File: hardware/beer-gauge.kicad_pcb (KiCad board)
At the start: 2 copper layers, 45 parts, among them P1 CONN_01X04, P2 CONN_01X04, P3 CONN_01X04, P4 CONN_01X04, P5 USB_OTG, SW1 SW_PUSH, U1 ADS1234IPW, U2 LP38691, U3 MKL02Z32, U4 MK20DX256VLH7, Y1 16 MHz, Y2 32.768 kHz

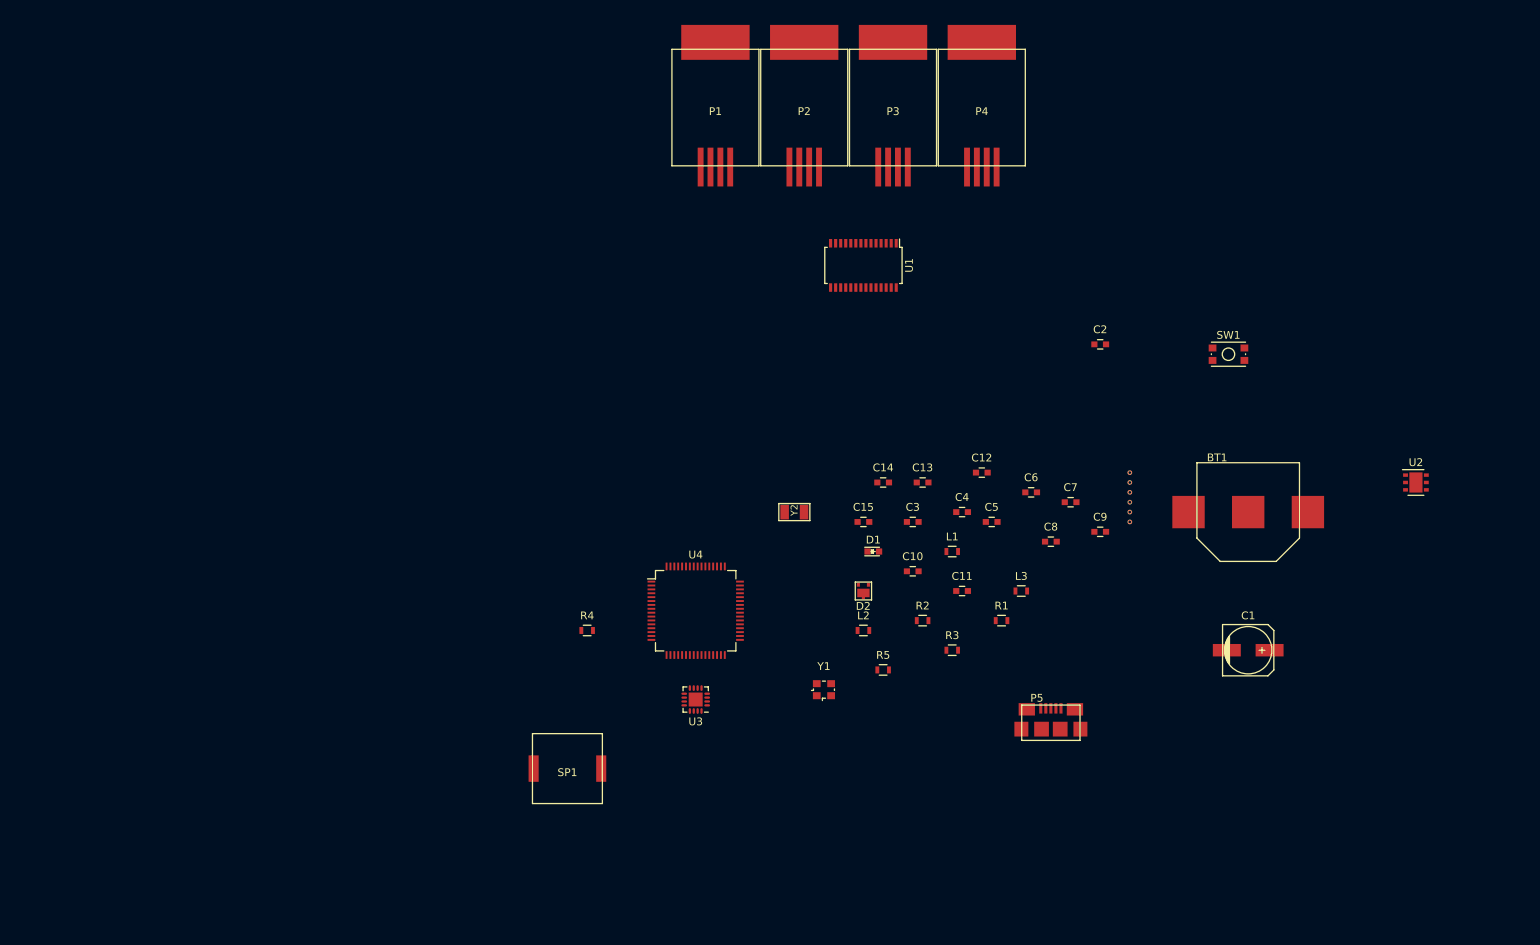
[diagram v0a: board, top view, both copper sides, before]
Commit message: Finished footprints.  Switched to a tantalum cap for the LCD.  Changed piezo resistor value to 470 to reduce part count.
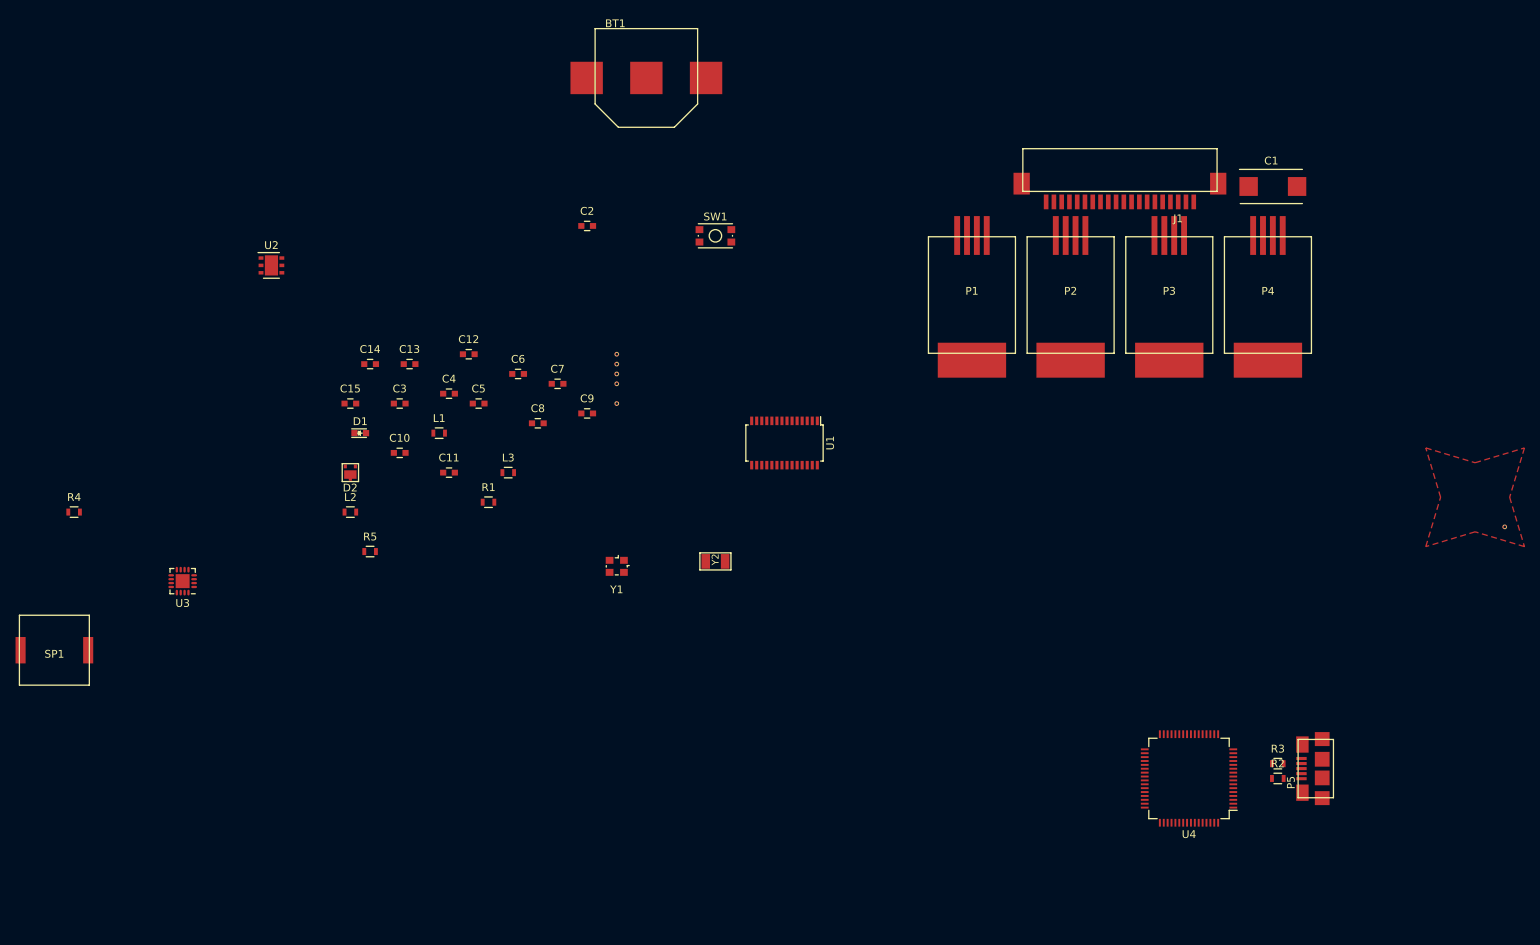
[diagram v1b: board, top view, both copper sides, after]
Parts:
- added J1: OLED_MODULE, footprint:0522712069, F.Cu at (165.1, 57.8)
- C1: footprint Capacitors_SMD:c_elec_6.3x5.8 -> Capacitors_Tantalum_SMD:TantalC_SizeD_EIA-7343_Reflow
- R5: value 1k -> 470
- moved U2 149.9 mm to (55.9, 67.3)
- moved BT1 95.5 mm to (104.1, 43.2)
- moved C10 67.8 mm to (72.4, 91.4)
- moved C11 67.8 mm to (78.7, 94.0)
- moved C14 67.8 mm to (68.6, 80.0)
- moved C15 67.8 mm to (66.0, 85.1)
- moved C2 67.8 mm to (96.5, 62.2)
- moved C3 67.8 mm to (72.4, 85.1)
- moved C4 67.8 mm to (78.7, 83.8)
- moved C5 67.8 mm to (82.5, 85.1)
- moved C7 67.8 mm to (92.7, 82.5)
- moved C8 67.8 mm to (90.2, 87.6)
- moved C9 67.8 mm to (96.5, 86.4)
- moved D2 67.8 mm to (66.0, 94.0)
- moved L2 67.8 mm to (66.0, 99.1)
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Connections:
- U4 pad 37: (no net) -> /Teensy/19/A5
- U4 pad 38: (no net) -> /Teensy/18/A4
- U4 pad 62: (no net) -> /Teensy/20/A6
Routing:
- added copper zone on F.Cu, net /Teensy/17/A3

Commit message: Working on capacitive touch arrow pad layout
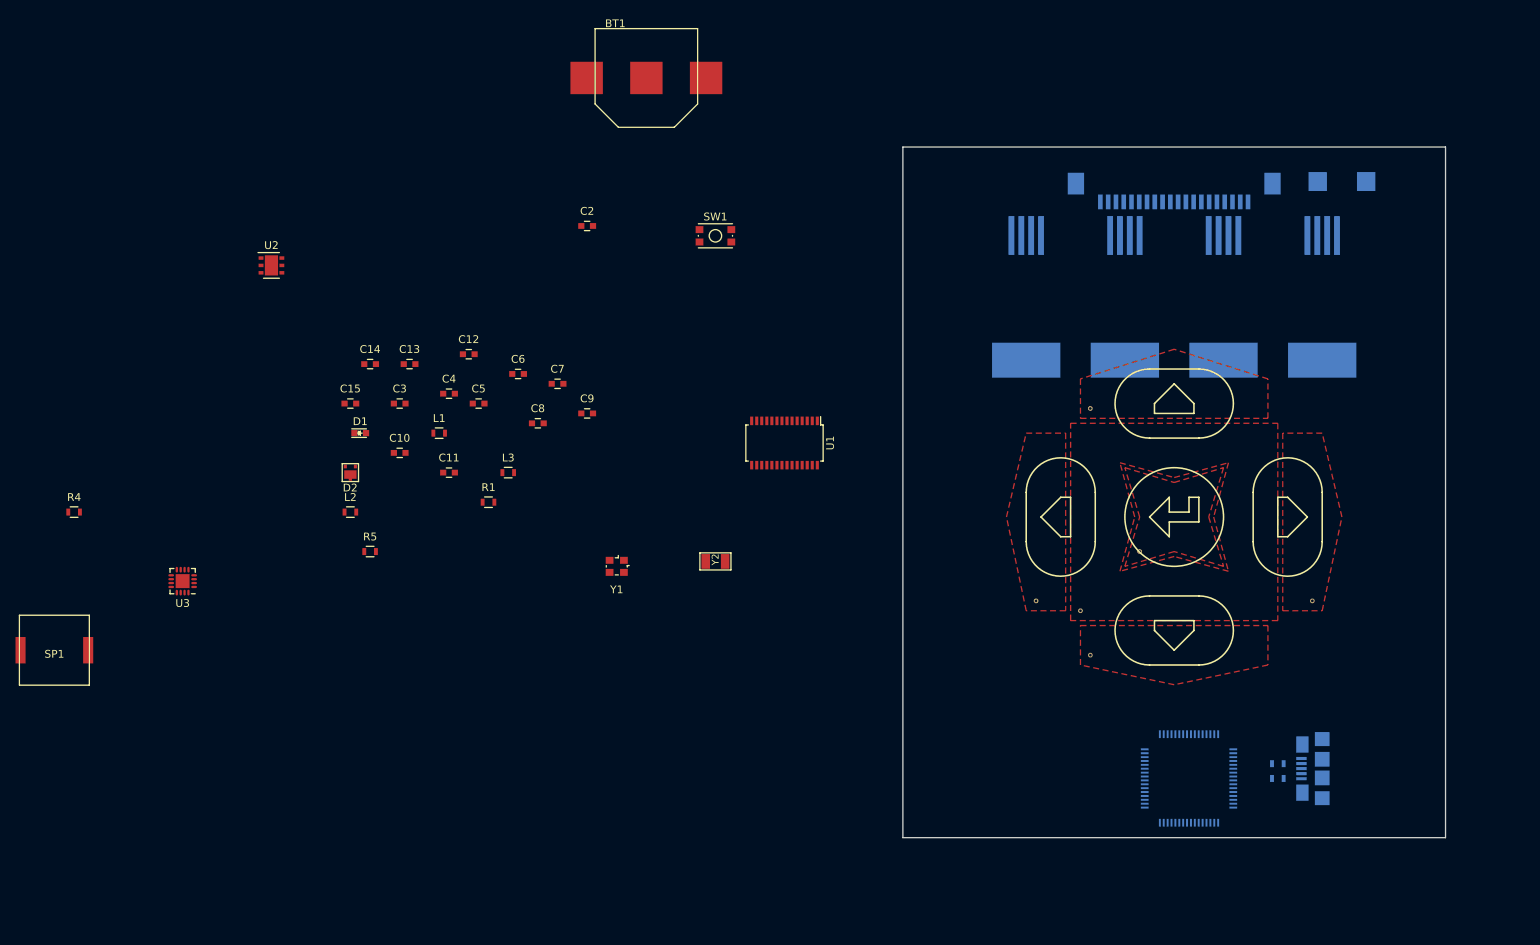
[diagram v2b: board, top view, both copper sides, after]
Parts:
- C1, J1, P1, P2, P3, P4, P5, R2, R3, U4: moved to B.Cu
- moved W4 93.8 mm to (189.9, 110.5)
- moved W2 71.6 mm to (161.3, 117.5)
- moved W6 65.4 mm to (160.0, 111.8)
- moved W3 61.4 mm to (154.3, 110.5)
- moved W1 61.4 mm to (161.3, 85.7)
- moved W5 47.1 mm to (167.6, 104.1)
- moved C1 8.91 mm to (193.7, 56.5)
- moved J1 6.99 mm to (172.1, 57.8), turned to 0 degrees
- moved P2 6.99 mm to (165.7, 71.1), turned to 0 degrees
- moved P3 6.99 mm to (178.4, 71.1), turned to 0 degrees
- moved P1 6.98 mm to (153.0, 71.1), turned to 0 degrees
- moved P4 6.98 mm to (191.1, 71.1), turned to 0 degrees
- turned P5 to 270 degrees
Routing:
- added copper zone on F.Cu, net /Teensy/15/A1
- added copper zone on F.Cu, net /Teensy/16/A2
- added copper zone on F.Cu, net /Teensy/22/A8
- added copper zone on F.Cu, net /Teensy/23/A9
- added copper zone on F.Cu, net /Teensy/25
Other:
- board outline added: 69.8 x 88.9 mm

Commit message: Working on component placement
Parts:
- moved P1 47.0 mm to (200.0, 71.1)
- moved P4 47.0 mm to (144.1, 71.1)
- moved P3 22.9 mm to (155.6, 71.1)
- moved P2 22.9 mm to (188.6, 71.1)
- moved P5 14.0 mm to (205.1, 130.8)
- moved R2 12.8 mm to (198.1, 132.1)
- moved R3 12.8 mm to (198.1, 130.2)
- moved W1 3.86 mm to (161.9, 81.9)
- moved W3 2.69 mm to (152.4, 108.6)
- moved W4 2.69 mm to (191.8, 108.6)
- moved U4 2.29 mm to (172.7, 131.4)
- moved W6 1.27 mm to (160.0, 110.5)
- moved W5 1.27 mm to (167.6, 102.9)
- moved W2 0.90 mm to (161.9, 118.1)
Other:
- net class Default: clearance 0.2 -> 0.1524; trace_width 0.25 -> 0.1524; via_dia 0.6 -> 0.508; via_drill 0.4 -> 0.3302
- rule trace_clearance: 0.2 -> 0.1524
- rule trace_min: 0.2 -> 0.1524
- rule via_min_drill: 0.3 -> 0.3302
- rule via_min_size: 0.4 -> 0.508

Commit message: Working on PCB layout
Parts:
- BT1, C10, C11, C12, C13, C14, C15, C2, C3, C4, C5, C6, C7, C8, C9, D1, D2, L1, L2, L3, R1, R4, R5, SP1, SW1, U1, U2, U3, Y1, Y2: moved to B.Cu
- moved U2 155.7 mm to (201.9, 121.3)
- moved U3 134.2 mm to (176.5, 131.4), turned to 270 degrees
- moved SP1 115.0 mm to (142.9, 119.4), turned to 270 degrees
- moved D2 103.4 mm to (159.4, 138.4), turned to 270 degrees
- moved BT1 101.1 mm to (149.9, 133.3)
- moved SW1 91.8 mm to (169.5, 135.9)
- moved Y2 90.5 mm to (197.5, 137.8), turned to 90 degrees
- moved Y1 84.1 mm to (178.4, 137.2)
- moved U1 79.6 mm to (201.3, 83.8), turned to 0 degrees
- moved C12 78.6 mm to (108.6, 152.4)
- moved C13 76.2 mm to (101.0, 151.1)
- moved C14 76.2 mm to (95.9, 151.1)
- moved C6 73.8 mm to (114.9, 149.9)
- moved R4 72.5 mm to (85.1, 146.7)
- moved C7 71.5 mm to (120.0, 148.6)
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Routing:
- added copper zone on B.Cu, net GND
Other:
- board size 69.8 x 88.9 mm -> 69.8 x 95.2 mm

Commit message: Working on PCB layout
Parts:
- added REF**: MountingHole_3.2mm_M3_Pad, Mounting_Holes:MountingHole_3.2mm_M3_Pad, F.Cu at (202.6, 50.2)
- added REF**: MountingHole_3.2mm_M3_Pad, Mounting_Holes:MountingHole_3.2mm_M3_Pad, F.Cu at (141.6, 50.2)
- added REF**: MountingHole_3.2mm_M3_Pad, Mounting_Holes:MountingHole_3.2mm_M3_Pad, F.Cu at (141.6, 136.5)
- added REF**: MountingHole_3.2mm_M3_Pad, Mounting_Holes:MountingHole_3.2mm_M3_Pad, F.Cu at (202.6, 136.5)
- moved R4 131.9 mm to (203.1, 87.6), turned to 90 degrees
- moved C15 126.9 mm to (203.7, 83.4)
- moved L2 117.1 mm to (203.7, 93.0)
- moved D1 116.7 mm to (205.0, 104.4), turned to 180 degrees
- moved C14 115.0 mm to (186.1, 79.8), turned to 180 degrees
- moved C10 114.7 mm to (203.7, 91.3)
- moved C13 113.0 mm to (199.0, 95.0)
- moved C11 112.8 mm to (203.7, 80.6)
- moved L3 104.0 mm to (203.7, 85.1)
- moved C8 103.7 mm to (204.7, 87.5), turned to 270 degrees
- moved C12 101.8 mm to (190.4, 91.8), turned to 180 degrees
- moved L1 96.8 mm to (200.8, 130.3), turned to 270 degrees
- moved C5 95.8 mm to (201.5, 118.4), turned to 90 degrees
- moved R1 95.4 mm to (202.1, 104.4)
- moved R5 94.2 mm to (179.2, 82.9), turned to 90 degrees
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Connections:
- net Net-(R2-Pad1) renamed /Teensy/USB_D-
- net Net-(R3-Pad1) renamed /Teensy/USB_D+
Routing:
- net +5V: track 0.00 -> 163.3 mm, vias 0 -> 8
- net /Teensy/16/A2: track 0.00 -> 96.0 mm, vias 0 -> 2
- net /Teensy/17/A3: track 0.00 -> 60.4 mm, vias 0 -> 2
- net /Teensy/22/A8: track 0.00 -> 54.5 mm, vias 0 -> 2
- net /Teensy/USB_D-: track 0.00 -> 53.8 mm
- net /Teensy/USB_D+: track 0.00 -> 53.6 mm
- net /Teensy/25: track 0.00 -> 51.1 mm, vias 0 -> 2
- net Net-(P2-Pad2): track 0.00 -> 40.9 mm
- net Net-(P2-Pad3): track 0.00 -> 40.4 mm
- net /Teensy/2: track 0.00 -> 39.5 mm, vias 0 -> 2
- net /Teensy/14/A0: track 0.00 -> 39.4 mm
- net /Teensy/12: track 0.00 -> 34.7 mm
- net /Teensy/23/A9: track 0.00 -> 34.4 mm, vias 0 -> 2
- net /Teensy/15/A1: track 0.00 -> 27.0 mm
- net Net-(P4-Pad3): track 0.00 -> 25.8 mm
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- added copper zone on In1.Cu, net +3V3
- added copper zone on In2.Cu, net GND
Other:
- outline, holes or cut-outs redrawn
- copper layers 2 -> 4
- net class 90Ohm added: clearance 0.127, trace_width 0.2286, via_dia 0.3556, via_drill 0.254
- net class Default: clearance 0.1524 -> 0.127; trace_width 0.1524 -> 0.127; via_dia 0.508 -> 0.3556; via_drill 0.3302 -> 0.254
- net class Power added: clearance 0.2032, trace_width 0.3556, via_dia 0.508, via_drill 0.4064
- rule trace_clearance: 0.1524 -> 0.127
- rule trace_min: 0.1524 -> 0.127
- rule via_min_drill: 0.3302 -> 0.254
- rule via_min_size: 0.508 -> 0.3556

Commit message: Working on PCB layout
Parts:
- moved SW1 1.73 mm to (202.8, 108.8)
- moved D1 1.53 mm to (204.9, 102.9)
- moved C5 1.45 mm to (200.4, 117.5)
- moved C7 1.45 mm to (203.7, 114.6)
- moved U2 1.45 mm to (203.2, 117.2)
- moved R1 1.17 mm to (201.2, 103.6)
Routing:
- net Net-(P1-Pad2): track 0.00 -> 61.8 mm, vias 0 -> 2
- net Net-(P1-Pad3): track 0.00 -> 60.9 mm, vias 0 -> 2
- net /Teensy/20/A6: track 0.00 -> 54.1 mm
- net /Teensy/4: track 0.00 -> 53.6 mm, vias 0 -> 2
- net /Teensy/5: track 0.00 -> 49.8 mm, vias 0 -> 2
- net /Teensy/19/A5: track 0.00 -> 49.0 mm, vias 0 -> 4
- net /Teensy/18/A4: track 0.00 -> 48.5 mm, vias 0 -> 4
- net GND: track 14.6 -> 62.4 mm, vias 13 -> 40
- net /Teensy/3: track 0.00 -> 46.5 mm, vias 0 -> 4
- net /Teensy/0: track 0.00 -> 38.9 mm, vias 0 -> 4
- net /Teensy/1: track 0.00 -> 38.4 mm, vias 0 -> 4
- net Net-(P3-Pad2): track 0.00 -> 33.7 mm, vias 0 -> 2
- net Net-(P3-Pad3): track 0.00 -> 33.3 mm, vias 0 -> 2
- net /Teensy/6: track 0.00 -> 23.2 mm, vias 0 -> 2
- net +3V3: track 16.1 -> 38.9 mm, vias 5 -> 7
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- added copper zone on F.Cu, net GND
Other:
- net class Power removed

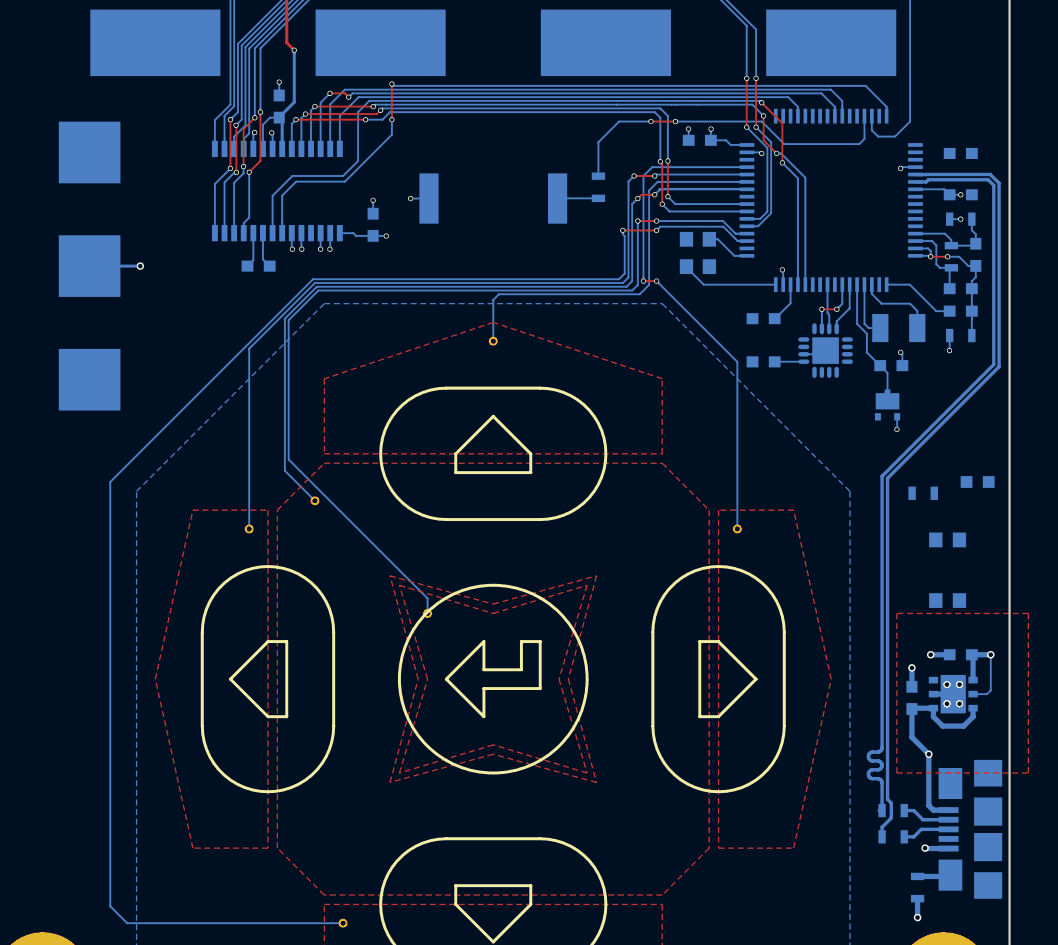
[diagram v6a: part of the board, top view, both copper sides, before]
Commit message: Finished routing traces
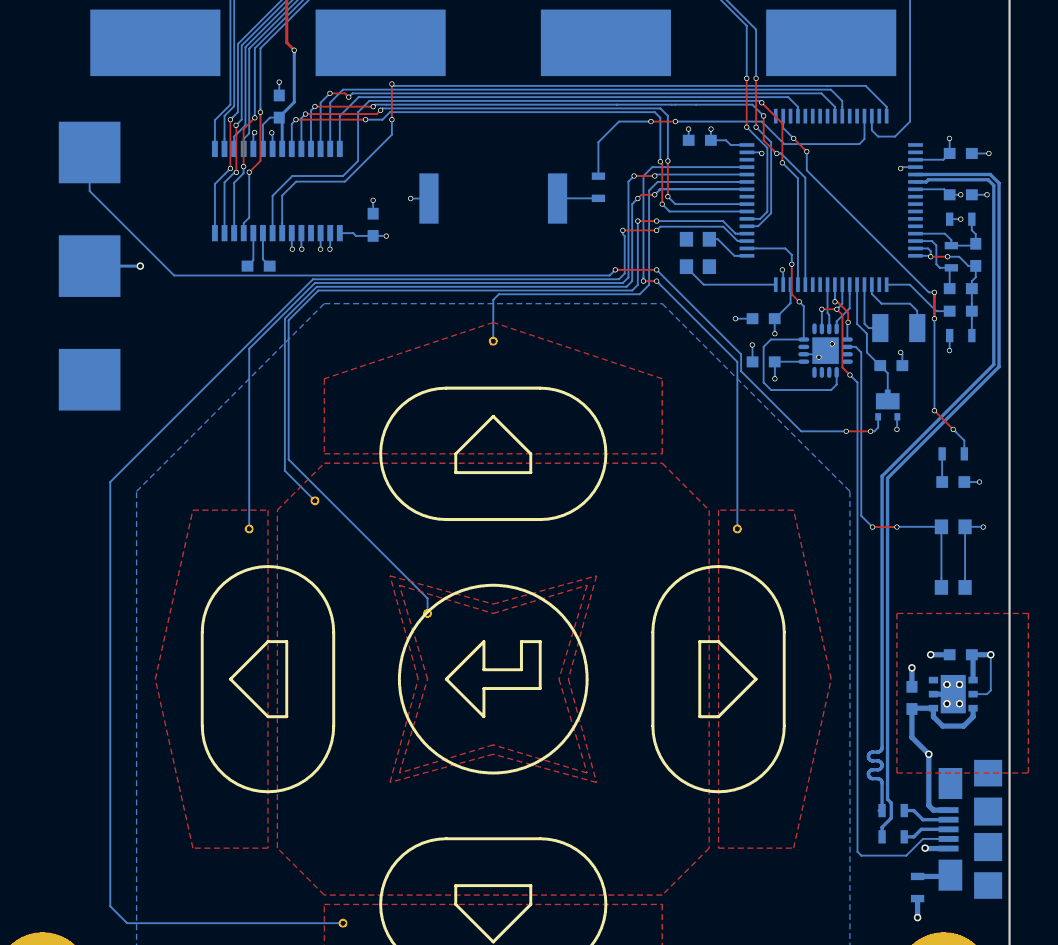
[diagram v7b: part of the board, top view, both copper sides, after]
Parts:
- moved R1 3.35 mm to (203.2, 101.0), turned to 180 degrees
- moved D1 1.65 mm to (203.2, 102.9)
- moved SW1 0.97 mm to (203.2, 108.0)
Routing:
- net Net-(BT1-Pad1): track 0.00 -> 64.5 mm, vias 0 -> 4
- net /Teensy/ID: track 4.16 -> 48.2 mm, vias 2 -> 3
- net /Teensy/13: track 0.00 -> 29.7 mm, vias 0 -> 6
- net Net-(SW1-Pad2): track 0.00 -> 22.0 mm, vias 0 -> 2
- net /Teensy/RESET_B: track 0.00 -> 20.7 mm, vias 0 -> 2
- net GND: track 62.4 -> 75.0 mm, vias 40 -> 48
- net +3V3: track 38.9 -> 44.6 mm, vias 7 -> 10
- net Net-(U3-Pad9): track 0.00 -> 4.20 mm, vias 0 -> 2
- net Net-(D1-Pad2): track 0.00 -> 1.91 mm

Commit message: Finished routing the board
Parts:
- added G***: LOGO, footprint:hatch_front, F.Cu at (172.1, 115.6)
- added G***: LOGO, footprint:hatch_back, F.Cu at (172.1, 115.6)
- added REF**: VIA, footprint:VIA, F.Cu at (148.1, 140.2)
- added REF**: VIA, footprint:VIA, F.Cu at (148.1, 103.5)
- added REF**: VIA, footprint:VIA, F.Cu at (196.1, 140.2)
- added REF**: VIA, footprint:VIA, F.Cu at (196.1, 103.5)
- added REF**: VIA, footprint:VIA, F.Cu at (183.5, 90.9)
- added REF**: VIA, footprint:VIA, F.Cu at (160.7, 90.9)
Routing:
- removed copper zone on B.Cu, net GND
- removed copper zone on F.Cu, net GND
